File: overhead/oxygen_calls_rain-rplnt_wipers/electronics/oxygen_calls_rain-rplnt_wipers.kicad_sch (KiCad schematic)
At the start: 83 parts, among them J1 Conn_02x01, J2 Conn_02x11_Counter_Clockwise, J3 Conn_02x01, J4 Conn_02x01, J5 Conn_02x01, J6 Conn_02x01, J7 Conn_02x01, J8 Conn_02x01, J9 Conn_02x02_Counter_Clockwise

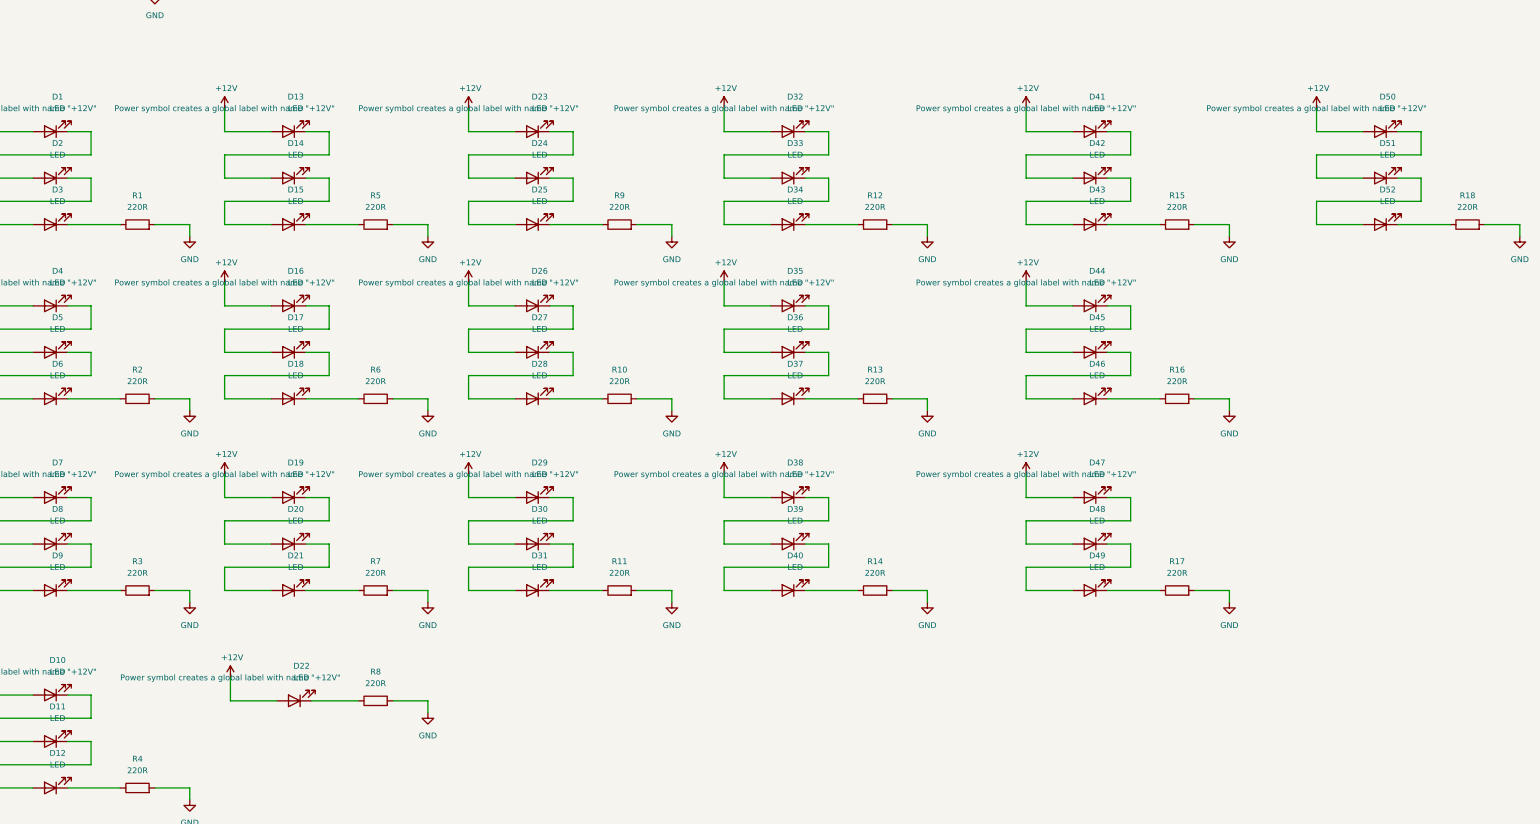
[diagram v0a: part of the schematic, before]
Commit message: Completed Oxygen_Calls_Rain Repellent & Wipers PCB + Changes to other designs
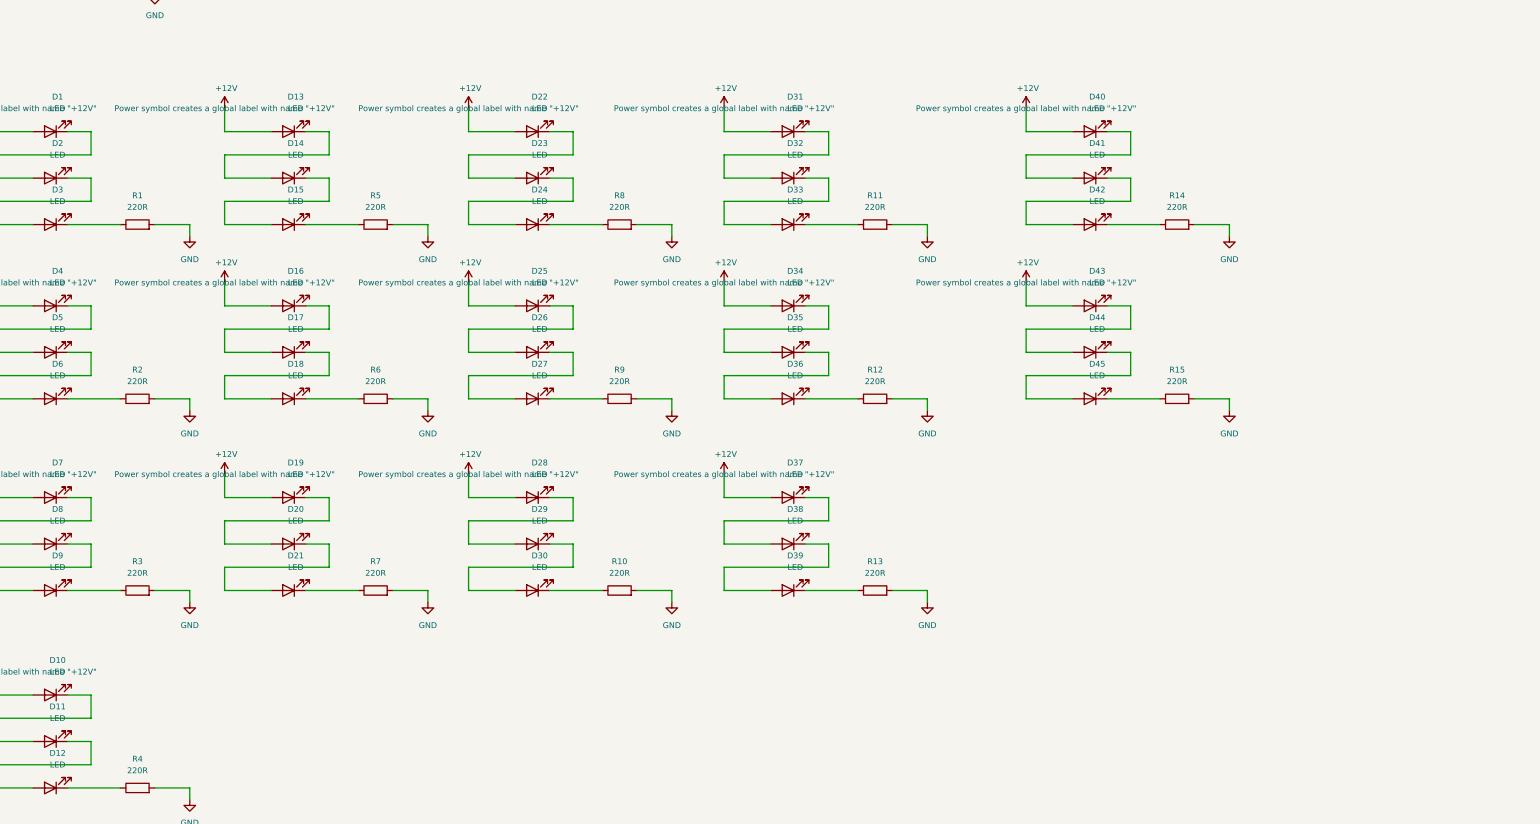
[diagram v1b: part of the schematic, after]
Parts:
- removed D22, D47, D48, D49, D50, D51, D52: LED, OpenA3XX:LED_Everlight-SMD3528_3.5x2.8mm_67-21ST, symbol Device:LED
- removed R17, R18, R8: 220R, Resistor_SMD:R_1206_3216Metric_Pad1.30x1.75mm_HandSolder, symbol Device:R
- renumbered D23 to D22, D24 to D23, D25 to D24, D26 to D25, D27 to D26, D28 to D27, D29 to D28, D30 to D29, D31 to D30, D32 to D31, D33 to D32, D34 to D33, D35 to D34, D36 to D35, D37 to D36, D38 to D37, D39 to D38, D40 to D39, D41 to D40, D42 to D41, D43 to D42, D44 to D43, D45 to D44, D46 to D45, R11 to R10, R12 to R11, R13 to R12, R14 to R13, R15 to R14, R16 to R15, R9 to R8, R10 to R9
